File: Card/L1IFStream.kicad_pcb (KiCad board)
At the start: 4 copper layers, 88.9 x 50.8 mm, 111 parts, among them J1 Conn_Coaxial, J2 USB_A, J3 RF_Shield_One_Piece, J4 Conn_Coaxial, U1 MAX2769BETI+T, U10 74LVC374, U11 74HC2GU04, U2 TPS717285DCK, U3 TPS717285DCK, U4 NCP164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

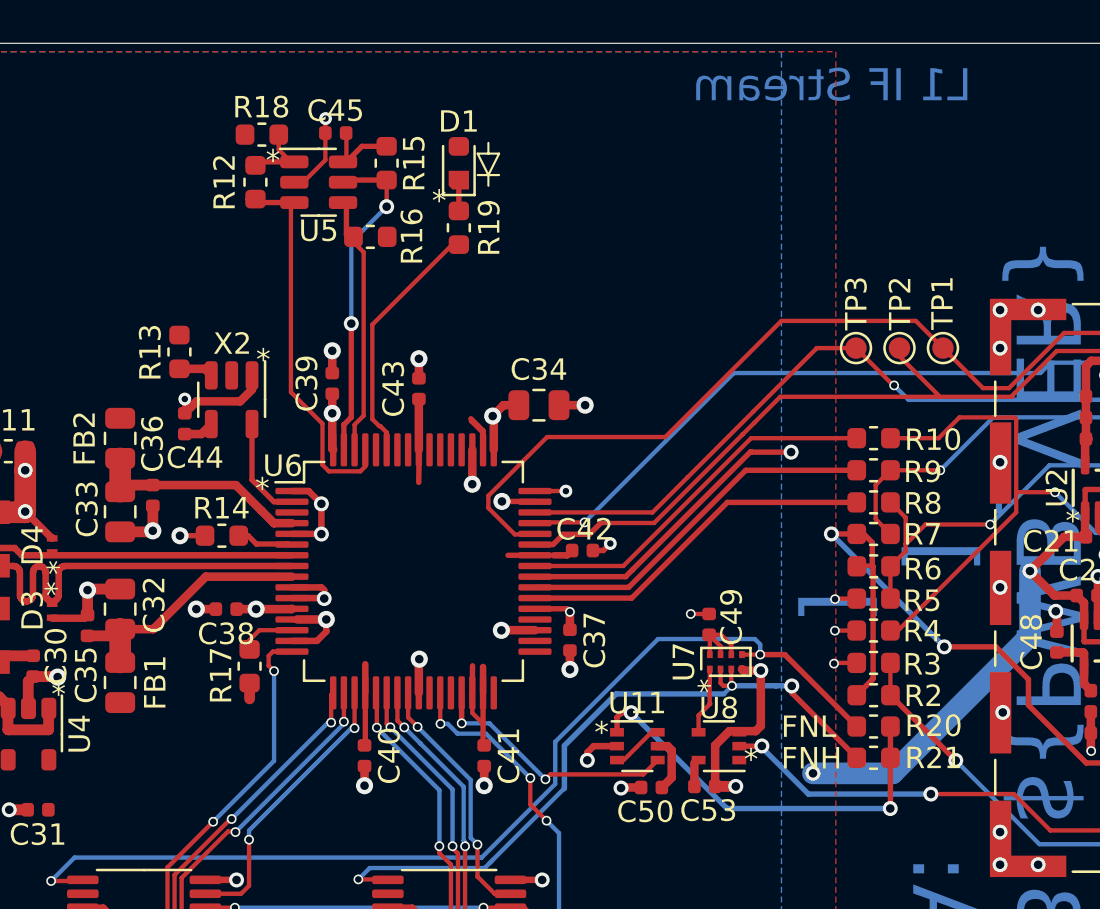
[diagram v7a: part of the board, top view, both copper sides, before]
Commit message: Library cleaned up through resistors. Just caps to go.
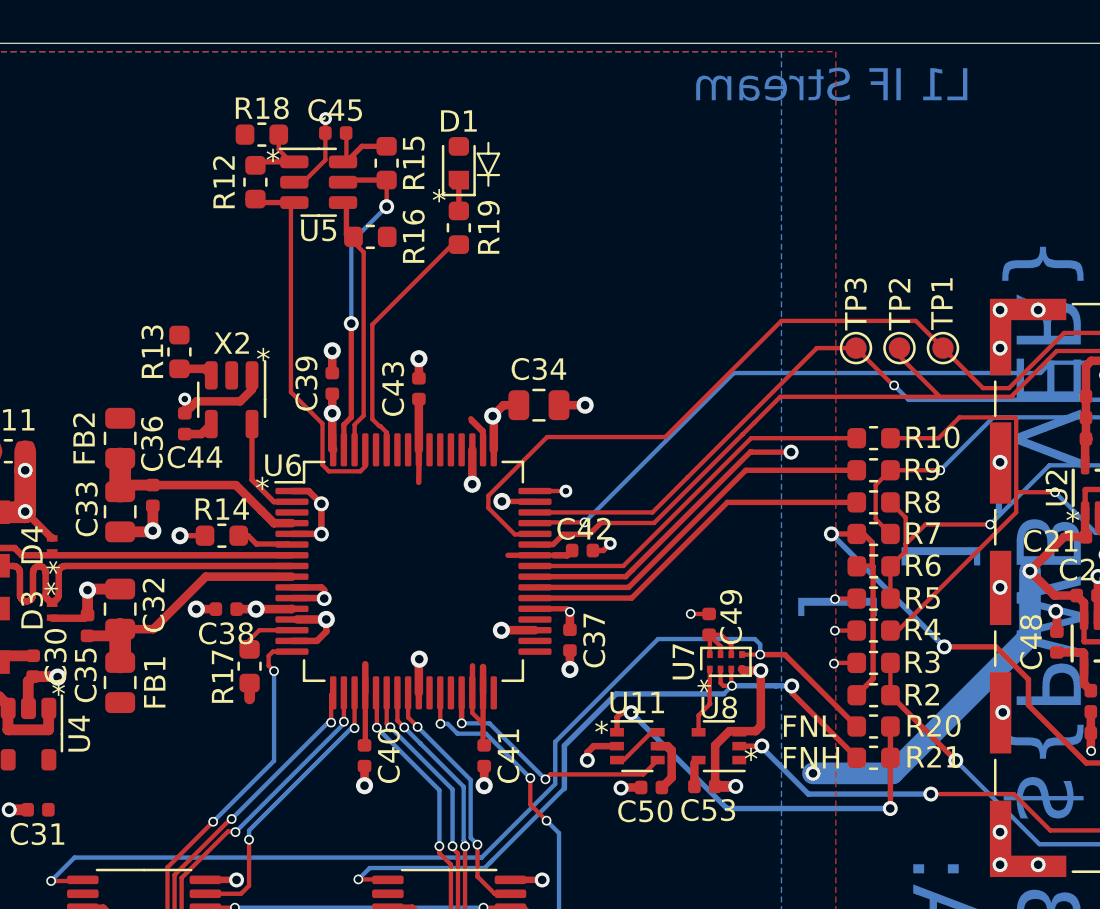
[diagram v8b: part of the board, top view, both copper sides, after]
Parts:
- R1, R10, R11, R12, R13, R14, R15, R16, R17, R18, R19, R2, R20, R21, R3, R4, R5, R6, R7, R8, R9: footprint L1IFStream:R_0603_1608Metric -> L1IF:R_0603_1608Metric
